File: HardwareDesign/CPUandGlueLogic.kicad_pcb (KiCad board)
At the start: 2 copper layers, 150 x 90 mm, 35 parts, among them J001 Conn_02x40_Odd_Even, J100 Conn_01x02, U101 74HCT245, U102 74HCT245, U103 74HCT245, U104 74HCT365, U105 MAX708, U106 HD6809, U107 74HCT00, U108 74HCT27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

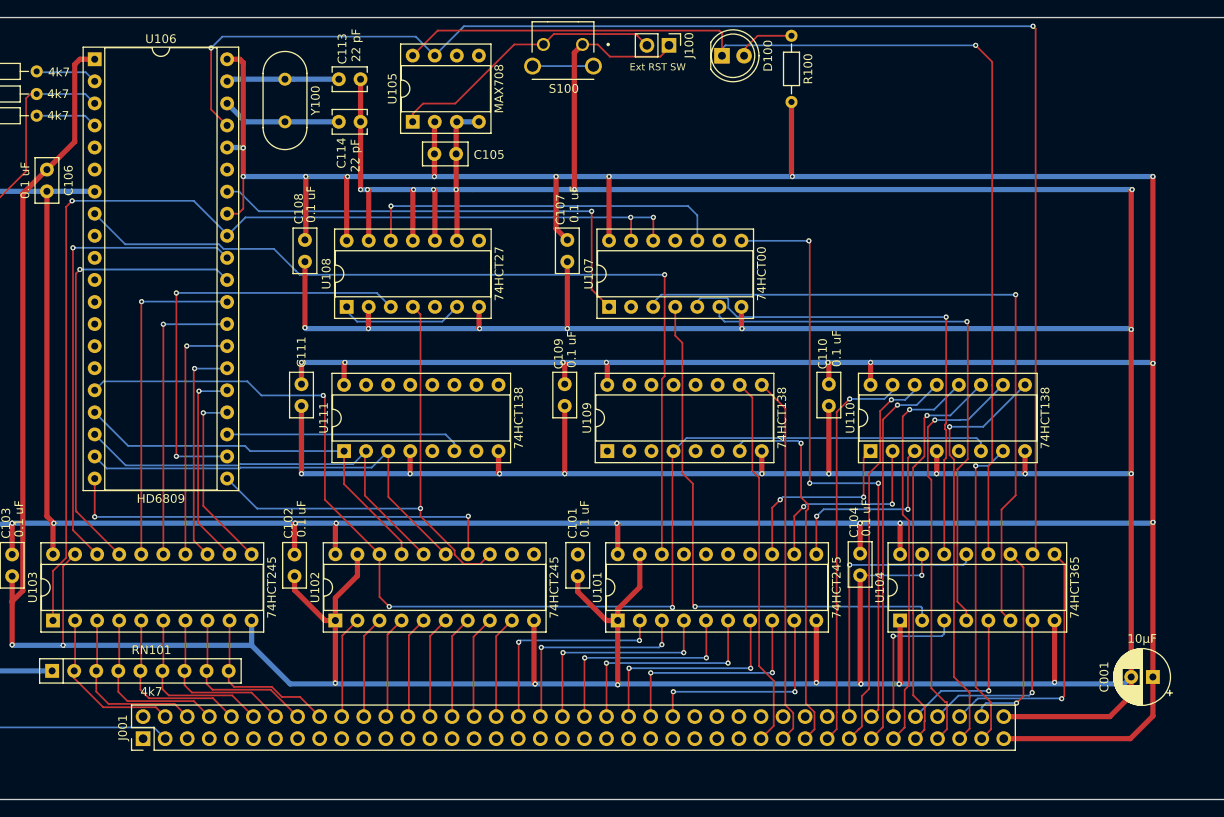
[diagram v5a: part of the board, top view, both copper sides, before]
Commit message: routed all signals, added holes for connector brackets
Still need to add ground planes.
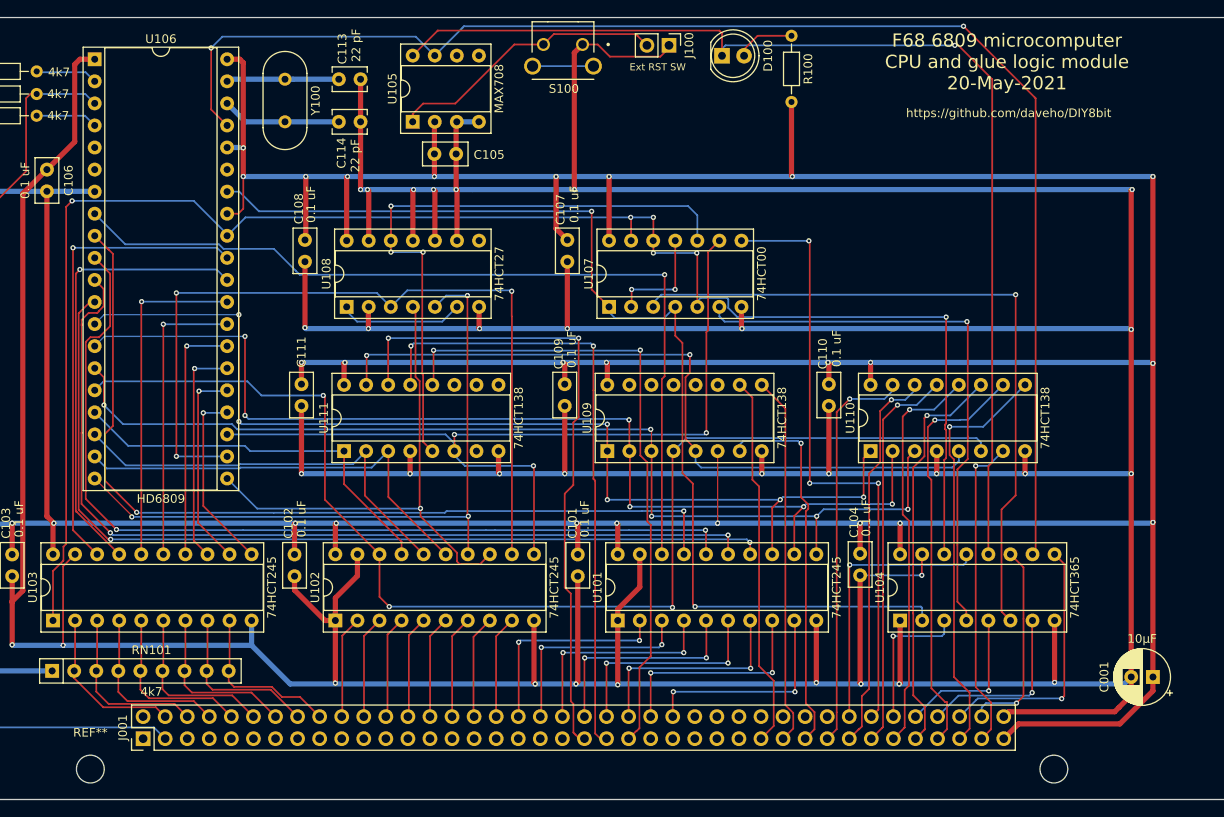
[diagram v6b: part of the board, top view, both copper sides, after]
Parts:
- added REF**: MountingHole_3.2mm_M3, MountingHole:MountingHole_3.2mm_M3, F.Cu at (19.4, 86.5)
- added REF**: MountingHole_3.2mm_M3, MountingHole:MountingHole_3.2mm_M3, F.Cu at (130.3, 86.5)
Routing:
- net /CPUandGlueLogic/Unbuf_A3: track 0.00 -> 106.1 mm, vias 0 -> 2
- net /CPUandGlueLogic/Unbuf_A2: track 0.00 -> 105.8 mm, vias 0 -> 2
- net /CPUandGlueLogic/Unbuf_A4: track 0.00 -> 105.2 mm, vias 0 -> 2
- net /CPUandGlueLogic/Unbuf_A1: track 0.00 -> 102.6 mm, vias 0 -> 2
- net /CPUandGlueLogic/Unbuf_A6: track 22.4 -> 123.7 mm, vias 2 -> 6
- net /CPUandGlueLogic/Unbuf_A5: track 22.0 -> 122.5 mm, vias 2 -> 6
- net /CPUandGlueLogic/Unbuf_A7: track 22.3 -> 120.1 mm, vias 2 -> 5
- net /CPUandGlueLogic/~IOR0~: track 0.00 -> 85.7 mm, vias 0 -> 2
- net /~IOR1~: track 0.00 -> 75.3 mm, vias 0 -> 2
- net /~IOR3~: track 0.00 -> 74.2 mm, vias 0 -> 2
- net /CPUandGlueLogic/Unbuf_A15: track 27.5 -> 101.5 mm, vias 0 -> 3
- net /~IOR2~: track 0.00 -> 72.0 mm, vias 0 -> 2
- net /CPUandGlueLogic/Unbuf_A14: track 50.0 -> 95.0 mm, vias 2 -> 3
- net Net-(U107-Pad10): track 42.6 -> 71.1 mm, vias 1 -> 3
- net /CPUandGlueLogic/Unbuf_A12: track 51.8 -> 79.1 mm, vias 2 -> 3
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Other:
- board text added: "F68 6809 microcomputer CPU and glue logic module 20-May-2021"
- board text added: "https://github.com/daveho/DIY8bit"

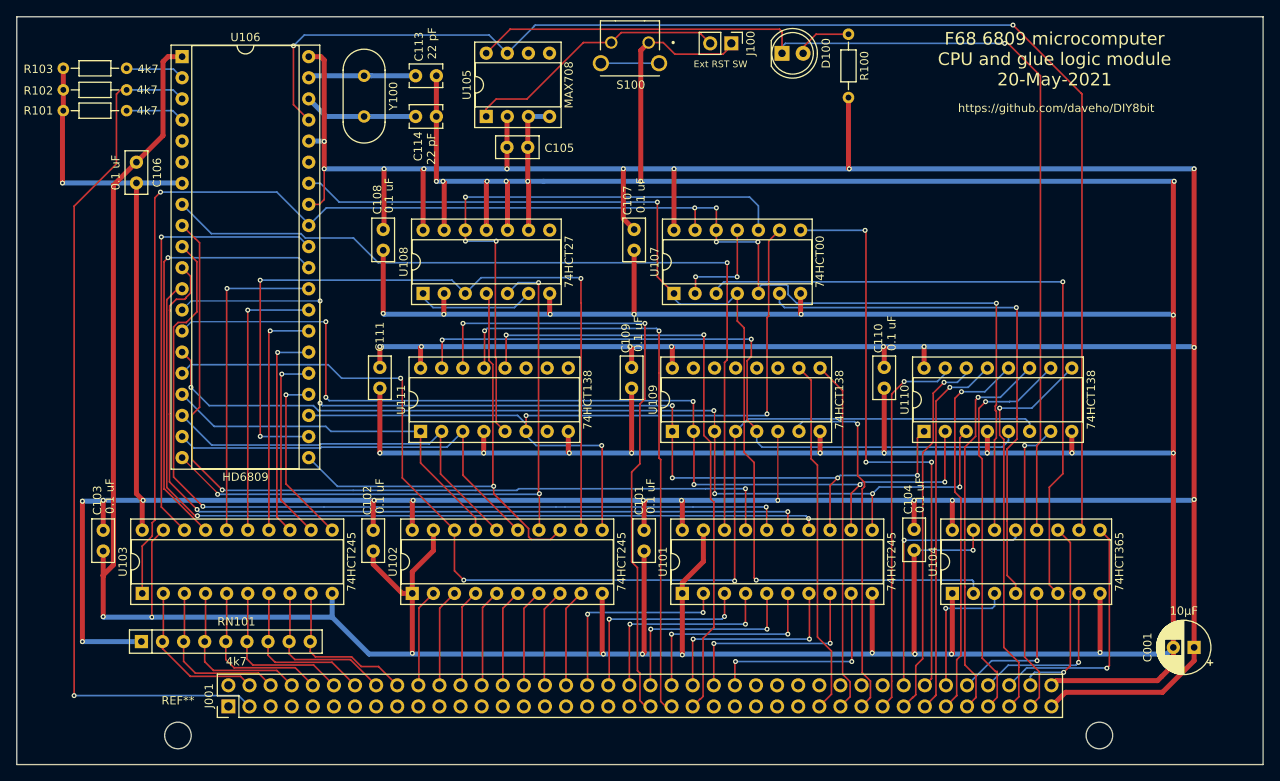
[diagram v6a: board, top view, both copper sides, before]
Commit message: added ground planes, slight adjustments to bracket holes
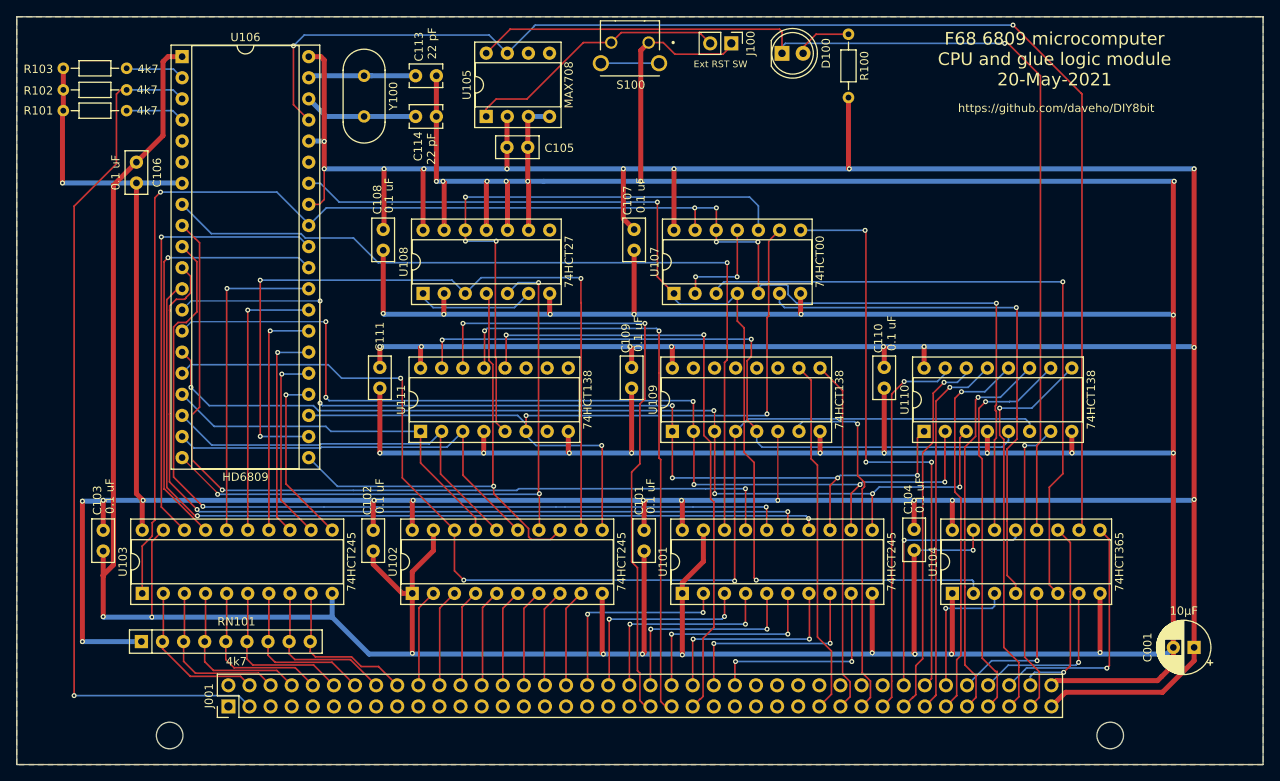
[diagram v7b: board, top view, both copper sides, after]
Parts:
- moved REF** 1.30 mm to (131.6, 86.5)
- moved REF** 1.00 mm to (18.4, 86.5)
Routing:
- added copper zone on B.Cu, net GND
- added copper zone on F.Cu, net GND
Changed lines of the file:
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@@
   )
   (module MountingHole:MountingHole_3.2mm_M3 (layer Front)
-    (at 19.4 86.5)
+    (at 18.4 86.5)
     (descr "Mounting Hole 3.2mm, no annular, M3")
     (tags "mounting hole 3.2mm no annular m3")
     (attr virtual)
-    (fp_text reference REF** (at 0 -4.2) (layer F.SilkS)
+    (fp_text reference REF** (at 0 -4.2) (layer F.Fab)
       (effects (font (size 1 1) (thickness 0.15)))
     )
@@
   )
   (module MountingHole:MountingHole_3.2mm_M3 (layer Front)
-    (at 130.3 86.5)
+    (at 131.6 86.5)
     (descr "Mounting Hole 3.2mm, no annular, M3")
     (tags "mounting hole 3.2mm no annular m3")
@@
   (segment (start 88.4 40.9) (end 88.4 38.8) (width 0.2) (layer Front) (net 129))
   (segment (start 87.9 41.4) (end 88.4 40.9) (width 0.2) (layer Front) (net 129))
+  (zone (net 2) (net_name GND) (layer Front) (hatch edge 0.508)
+    (connect_pads (clearance 0.508))
+    (min_thickness 0.254)
+    (fill yes (arc_segments 32) (thermal_gap 0.508) (thermal_bridge_width 0.508))
+    (polygon
+      (pts
+        (xy 150 90) (xy 0 90) (xy 0 0) (xy 150 0)
+      )
+    )
+  )
+  (zone (net 2) (net_name GND) (layer Back) (hatch edge 0.508)
+    (connect_pads (clearance 0.508))
+    (min_thickness 0.254)
+    (fill yes (arc_segments 32) (thermal_gap 0.508) (thermal_bridge_width 0.508))
+    (polygon
+      (pts
+        (xy 150 90) (xy 0 90) (xy 0 0) (xy 150 0)
+      )
+    )
+  )
 )
